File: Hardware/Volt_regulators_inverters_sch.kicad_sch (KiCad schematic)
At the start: 15 parts, among them IC1 MCP1754ST-3302E_DB, U11 LM2665M6, U6 TPS73133DBV, U7 TPS72325DBV, U8 TLV70310DBVR

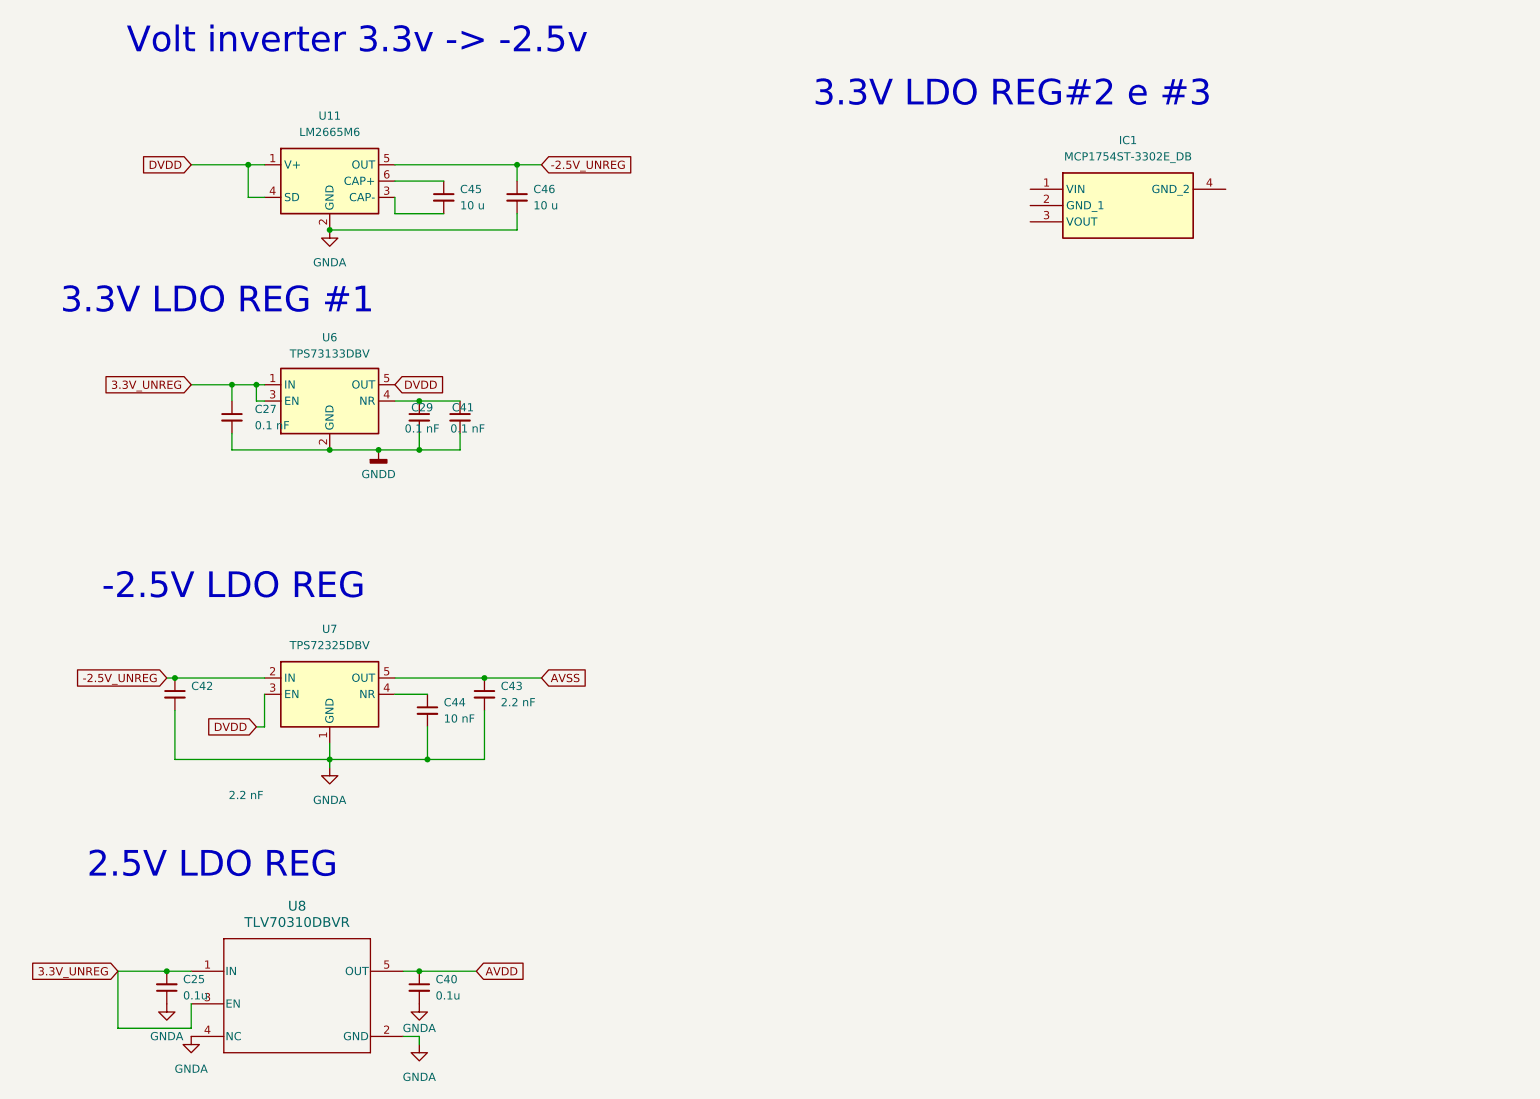
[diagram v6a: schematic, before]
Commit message: Remove redundant components
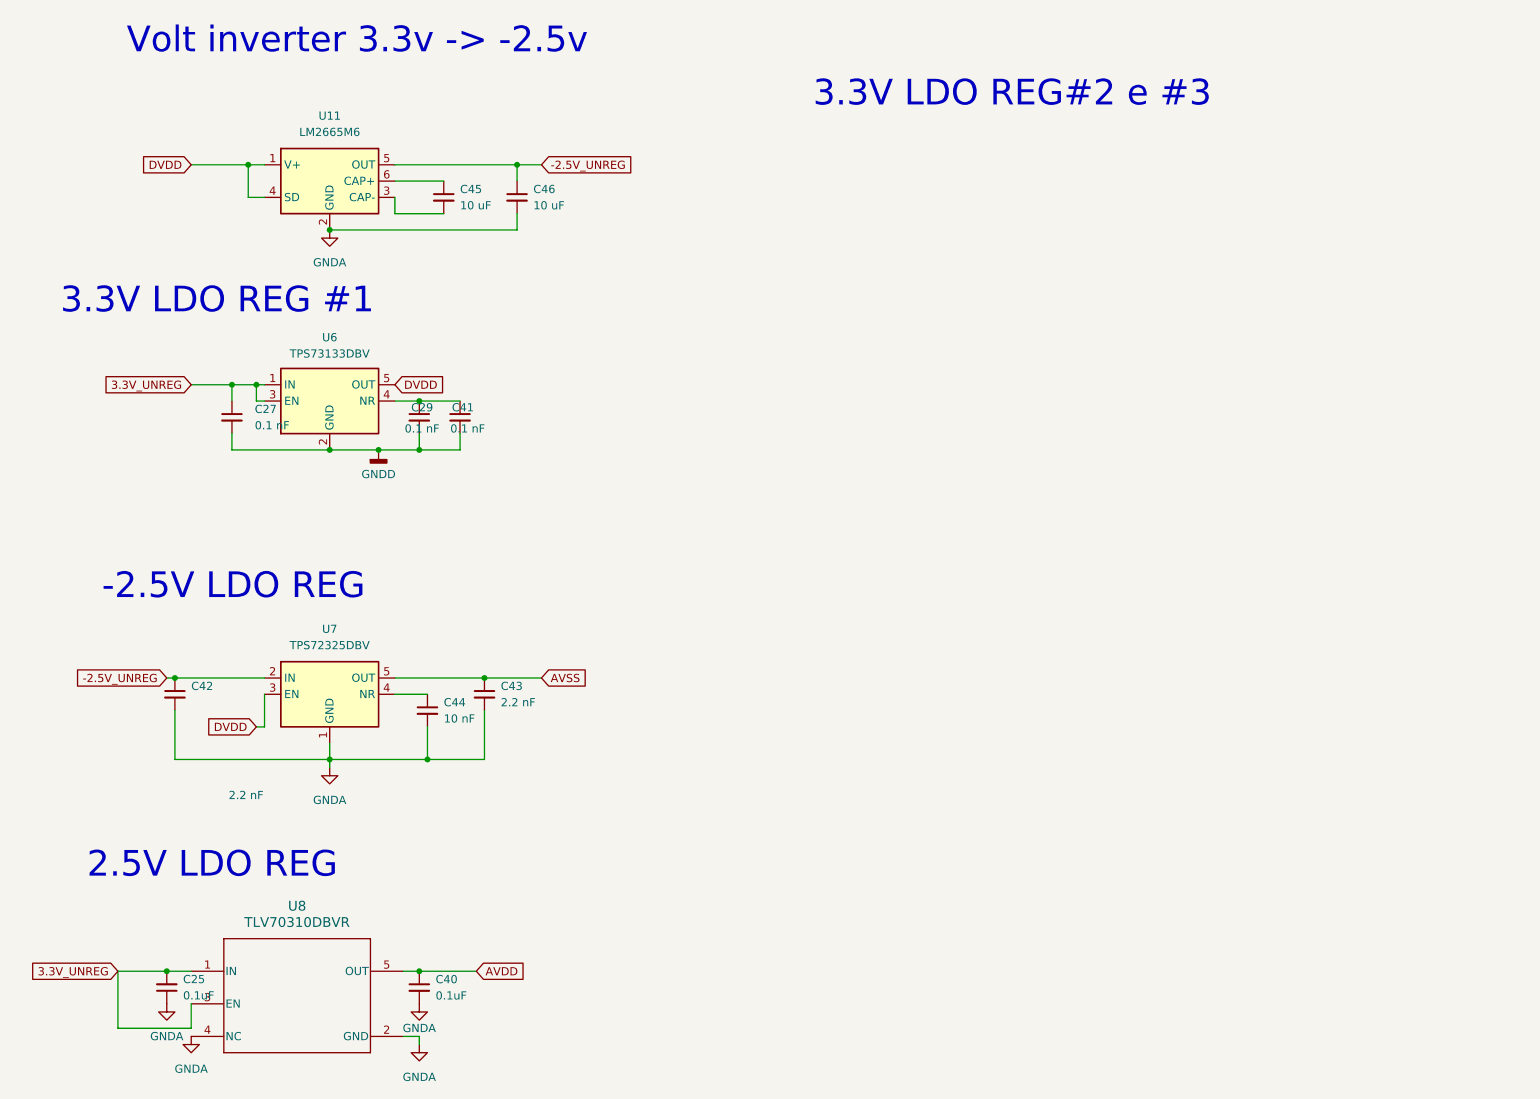
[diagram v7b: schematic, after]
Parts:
- removed IC1: MCP1754ST-3302E_DB, mcp1754:SOT230P700X180-4N, symbol Mcp1754:MCP1754ST-3302E_DB
- C25, C40: value 0.1u -> 0.1uF
- C45, C46: value 10 u -> 10 uF
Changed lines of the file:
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@@
 			)
 		)
-		(property "Value" "10 u"
+		(property "Value" "10 uF"
 			(at 81.28 44.4562 0)
 			(effects
@@
 	)
 	(symbol
-		(lib_id "Mcp1754:MCP1754ST-3302E_DB")
-		(at 170.18 41.91 0)
-		(unit 1)
-		(exclude_from_sim no)
-		(in_bom yes)
-		(on_board yes)
-		(dnp no)
-		(fields_autoplaced yes)
-		(property "Reference" "IC1"
-			(at 185.42 34.29 0)
-			(effects
-				(font
-					(size 1.27 1.27)
-				)
-			)
-		)
-		(property "Value" "MCP1754ST-3302E_DB"
-			(at 185.42 36.83 0)
-			(effects
-				(font
-					(size 1.27 1.27)
-				)
-			)
-		)
-		(property "Footprint" "mcp1754:SOT230P700X180-4N"
-			(at 196.85 136.83 0)
-			(effects
-				(font
-					(size 1.27 1.27)
-				)
-				(justify left top)
-				(hide yes)
-			)
-		)
-		(property "Datasheet" "http://www.microchip.com/mymicrochip/filehandler.aspx?ddocname=en555395"
-			(at 196.85 236.83 0)
-			(effects
-				(font
-					(size 1.27 1.27)
-				)
-				(justify left top)
-				(hide yes)
-			)
-		)
-		(property "Description" "LDO Voltage Regulators LDO"
-			(at 170.18 41.91 0)
-			(effects
-				(font
-					(size 1.27 1.27)
-				)
-				(hide yes)
-			)
-		)
-		(property "Height" "1.8"
-			(at 196.85 436.83 0)
-			(effects
-				(font
-					(size 1.27 1.27)
-				)
-				(justify left top)
-				(hide yes)
-			)
-		)
-		(property "Mouser Part Number" "579-MCP1754T-3302EDB"
-			(at 196.85 536.83 0)
-			(effects
-				(font
-					(size 1.27 1.27)
-				)
-				(justify left top)
-				(hide yes)
-			)
-		)
-		(property "Mouser Price/Stock" "https://www.mouser.co.uk/ProductDetail/Microchip-Technology/MCP1754ST-3302E-DB?qs=geWWqIMx8Ypn%2FSBmGzIfBw%3D%3D"
-			(at 196.85 636.83 0)
-			(effects
-				(font
-					(size 1.27 1.27)
-				)
-				(justify left top)
-				(hide yes)
-			)
-		)
-		(property "Manufacturer_Name" "Microchip"
-			(at 196.85 736.83 0)
-			(effects
-				(font
-					(size 1.27 1.27)
-				)
-				(justify left top)
-				(hide yes)
-			)
-		)
-		(property "Manufacturer_Part_Number" "MCP1754ST-3302E/DB"
-			(at 196.85 836.83 0)
-			(effects
-				(font
-					(size 1.27 1.27)
-				)
-				(justify left top)
-				(hide yes)
-			)
-		)
-		(pin "3"
-		)
-		(pin "1"
-		)
-		(pin "4"
-		)
-		(pin "2"
-		)
-		(instances
-			(project ""
-				(path "/59c54cdb-19a2-4654-a4c9-f1907d038780/db58efb1-7103-4a17-b794-0e1a9c461960"
-					(reference "IC1")
-					(unit 1)
-				)
-			)
-		)
-	)
-	(symbol
 		(lib_id "power:GNDA")
 		(at 74.93 175.26 0)
@@
 			)
 		)
-		(property "Value" "10 u"
+		(property "Value" "10 uF"
 			(at 92.71 44.4562 0)
 			(effects
@@
 			)
 		)
-		(property "Value" "0.1u"
+		(property "Value" "0.1uF"
 			(at 77.47 167.6462 0)
 			(effects
@@
 			)
 		)
-		(property "Value" "0.1u"
+		(property "Value" "0.1uF"
 			(at 38.1 167.6335 0)
 			(effects

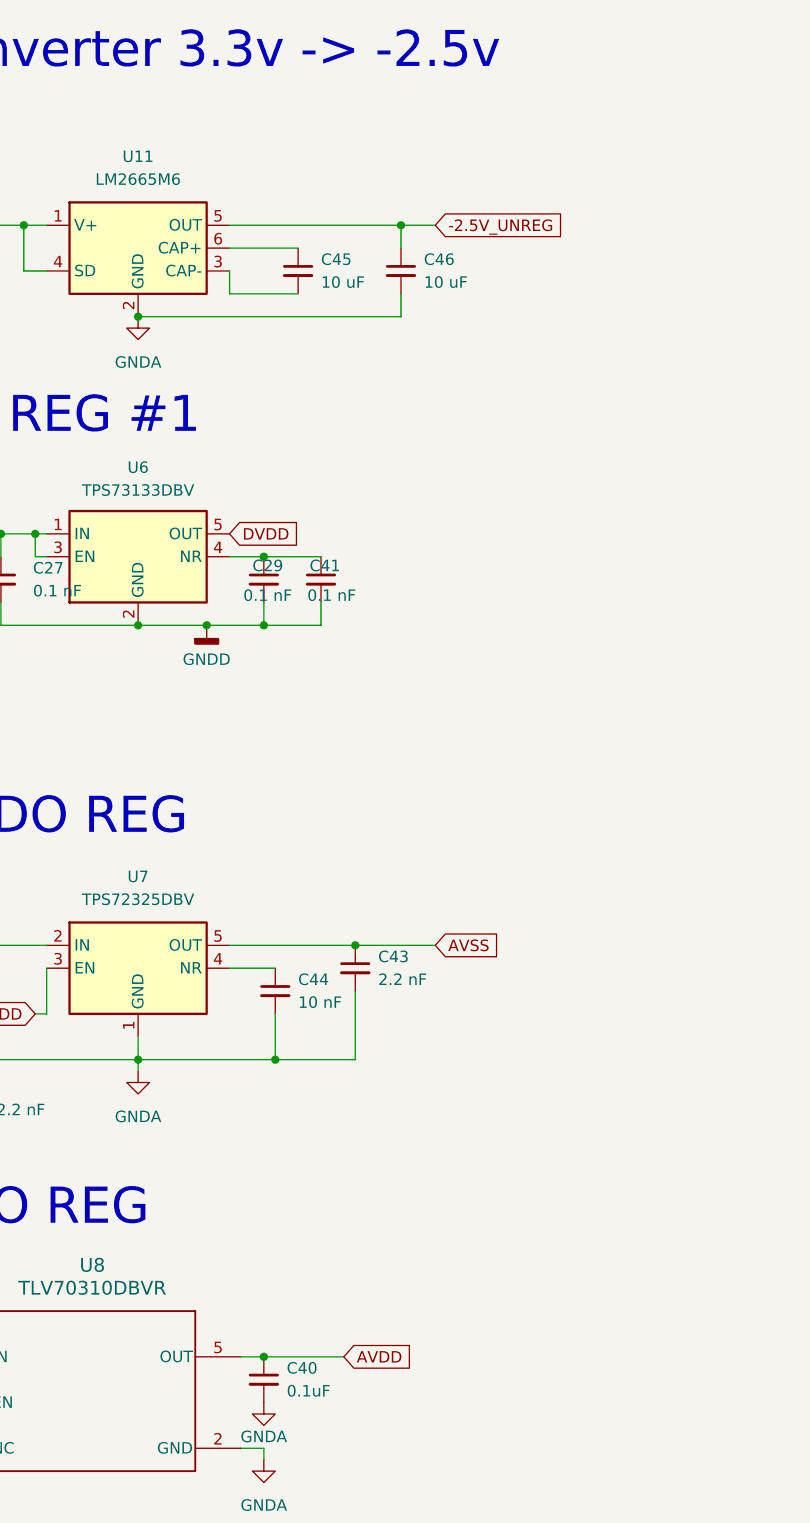
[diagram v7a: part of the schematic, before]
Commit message: Feat: fix small connection error, made board bigger
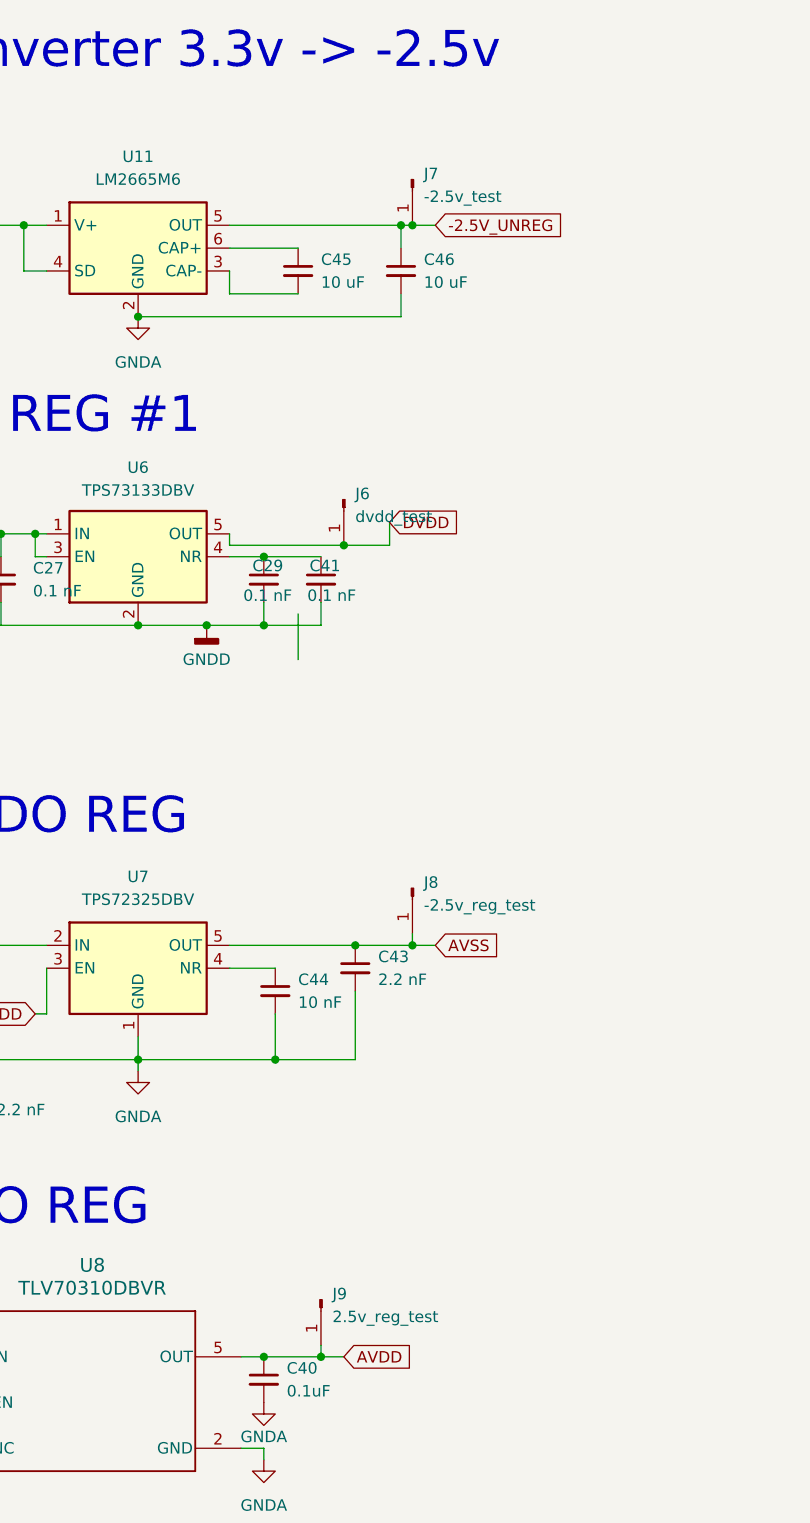
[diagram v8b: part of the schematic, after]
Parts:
- added J6: dvdd_test, Connector_PinHeader_2.54mm:PinHeader_1x01_P2.54mm_Vertical, symbol Connector:Conn_01x01_Pin
- added J7: -2.5v_test, Connector_PinHeader_2.54mm:PinHeader_1x01_P2.54mm_Vertical, symbol Connector:Conn_01x01_Pin
- added J8: -2.5v_reg_test, Connector_PinHeader_2.54mm:PinHeader_1x01_P2.54mm_Vertical, symbol Connector:Conn_01x01_Pin
- added J9: 2.5v_reg_test, Connector_PinHeader_2.54mm:PinHeader_1x01_P2.54mm_Vertical, symbol Connector:Conn_01x01_Pin
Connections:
- net -2.5V_UNREG: now also J7.1 (Pin_1)
- net AVDD: now also J9.1 (Pin_1)
- net AVSS: now also J8.1 (Pin_1)
- net DVDD: now also J6.1 (Pin_1)
